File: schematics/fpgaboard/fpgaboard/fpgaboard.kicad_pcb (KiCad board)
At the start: 6 copper layers, 67.6 x 37.5 mm, 17 parts, among them J1 SODIMM-200, U1 LFE5UM-85F-8BG381I, U13 W25Q32JVSS, U2 AMS1117-3.3, U3 IS42S16320F-7TL, U4 IS42S16320F-7TL

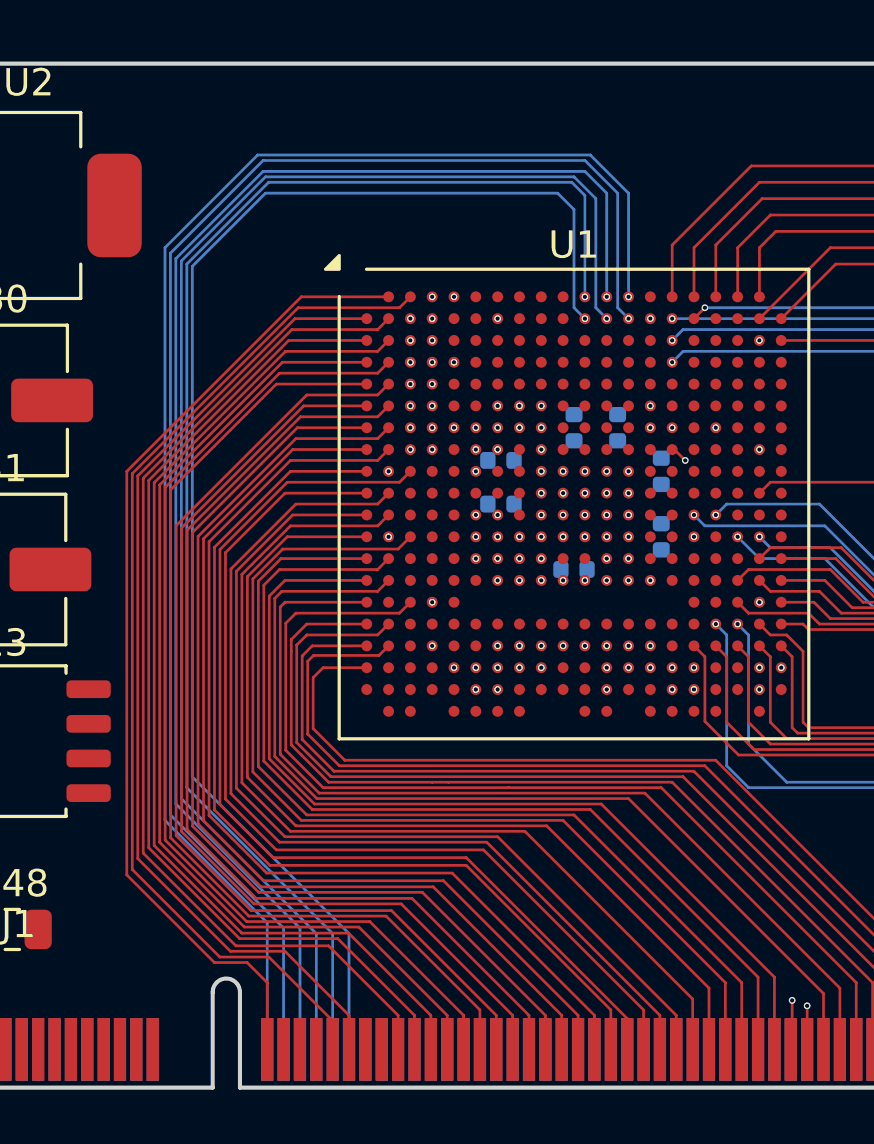
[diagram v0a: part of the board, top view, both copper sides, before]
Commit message: More work on FPGA board.
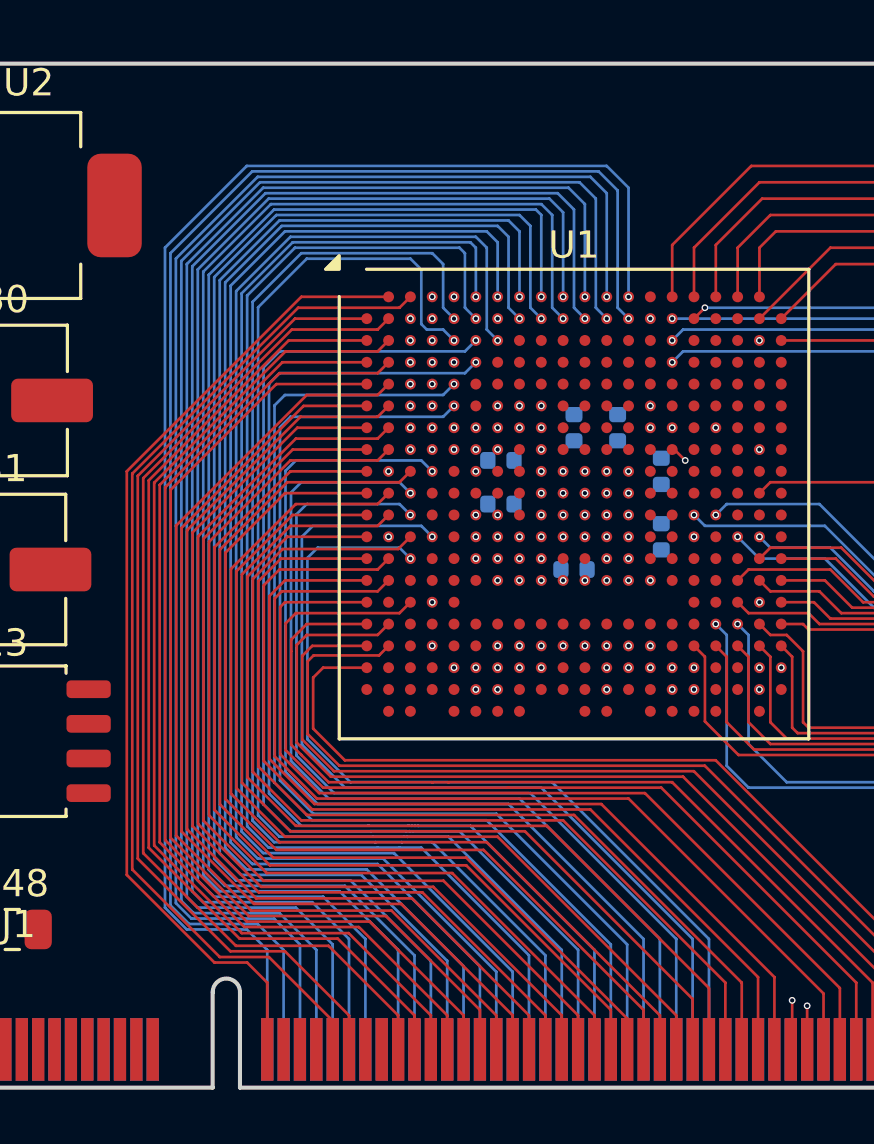
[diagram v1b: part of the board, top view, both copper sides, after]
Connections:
- U1 pad A10: unconnected-(U1B-PT63A-PadA10) -> S58
- U1 pad A6: unconnected-(U1B-PT4A-PadA6) -> S66
- U1 pad A7: unconnected-(U1B-PT18A-PadA7) -> S64
- U1 pad A8: unconnected-(U1B-PT18B-PadA8) -> S62
- U1 pad A9: unconnected-(U1B-PT60A-PadA9) -> S60
- U1 pad B10: unconnected-(U1B-PT60B-PadB10) -> S59
- U1 pad B5: unconnected-(U1G-PL11C-PadB5) -> S68
- U1 pad B6: unconnected-(U1B-PT4B-PadB6) -> S67
- U1 pad B8: unconnected-(U1B-PT15B-PadB8) -> S63
- U1 pad B9: unconnected-(U1B-PT58A-PadB9) -> S61
- U1 pad C5: unconnected-(U1G-PL11D-PadC5) -> S69
- U1 pad C6: unconnected-(U1B-PT11A-PadC6) -> S70
- U1 pad C7: unconnected-(U1B-PT11B-PadC7) -> S65
- U1 pad D6: unconnected-(U1B-PT6B-PadD6) -> S71
- U1 pad E5: unconnected-(U1G-PL20C-PadE5) -> S72
- U1 pad F5: unconnected-(U1G-PL20D-PadF5) -> S73
- U1 pad H5: unconnected-(U1G-PL41C-PadH5) -> S74
- U1 pad J4: unconnected-(U1F-PL50A-PadJ4) -> S74
- U1 pad K3: unconnected-(U1F-PL50D-PadK3) -> S75
- U1 pad L3: unconnected-(U1F-PL86C-PadL3) -> S76
- U1 pad M4: unconnected-(U1F-PL83A-PadM4) -> S77
- U1 pad N3: unconnected-(U1F-PL86A-PadN3) -> S78
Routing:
- net S59: track 0.00 -> 52.0 mm, vias 0 -> 1
- net S58: track 0.00 -> 51.3 mm, vias 0 -> 1
- net S60: track 0.00 -> 50.4 mm, vias 0 -> 1
- net S61: track 0.00 -> 50.3 mm, vias 0 -> 1
- net S63: track 0.00 -> 48.9 mm, vias 0 -> 1
- net S62: track 0.00 -> 48.7 mm, vias 0 -> 1
- net S65: track 0.00 -> 48.2 mm, vias 0 -> 1
- net S64: track 0.00 -> 47.3 mm, vias 0 -> 1
- net S67: track 0.00 -> 46.6 mm, vias 0 -> 1
- net S66: track 0.00 -> 45.9 mm, vias 0 -> 1
- net S69: track 0.00 -> 45.8 mm, vias 0 -> 1
- net S68: track 0.00 -> 45.3 mm, vias 0 -> 1
- net S70: track 0.00 -> 41.6 mm, vias 0 -> 1
- net S71: track 0.00 -> 40.9 mm, vias 0 -> 1
- net S72: track 0.00 -> 39.4 mm, vias 0 -> 1
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
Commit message: Some work on FPGA board.
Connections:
- U1 pad D7: unconnected-(U1B-PT9B-PadD7) -> S86
- U1 pad E6: unconnected-(U1B-PT6A-PadE6) -> S85
- U1 pad J4: S74 -> S75
- U1 pad K3: S75 -> S76
- U1 pad K4: unconnected-(U1F-PL56A-PadK4) -> S77
- U1 pad L3: S76 -> S78
- U1 pad L4: unconnected-(U1F-PL56C-PadL4) -> S79
- U1 pad M4: S77 -> S80
- U1 pad N3: S78 -> S81
- U1 pad N4: unconnected-(U1F-PL83C-PadN4) -> S82
- U1 pad N5: unconnected-(U1F-PL83B-PadN5) -> S83
- U1 pad P5: unconnected-(U1F-PL83D-PadP5) -> S84
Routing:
- net S86: track 0.00 -> 37.5 mm, vias 0 -> 2
- net S85: track 0.00 -> 36.7 mm, vias 0 -> 2
- net S83: track 0.00 -> 34.8 mm, vias 0 -> 1
- net S84: track 0.00 -> 34.6 mm, vias 0 -> 1
- net S79: track 0.00 -> 34.2 mm, vias 0 -> 1
- net S80: track 0.00 -> 33.7 mm, vias 0 -> 1
- net S82: track 0.00 -> 33.3 mm, vias 0 -> 1
- net S81: track 0.00 -> 32.5 mm, vias 0 -> 1
- net S78: track 32.6 -> 33.5 mm
- net S77: track 34.1 -> 34.8 mm
- net S70: track 41.6 -> 41.0 mm
- net S75: track 34.8 -> 35.3 mm
- net S74: track 36.5 -> 36.8 mm, vias 2 -> 1

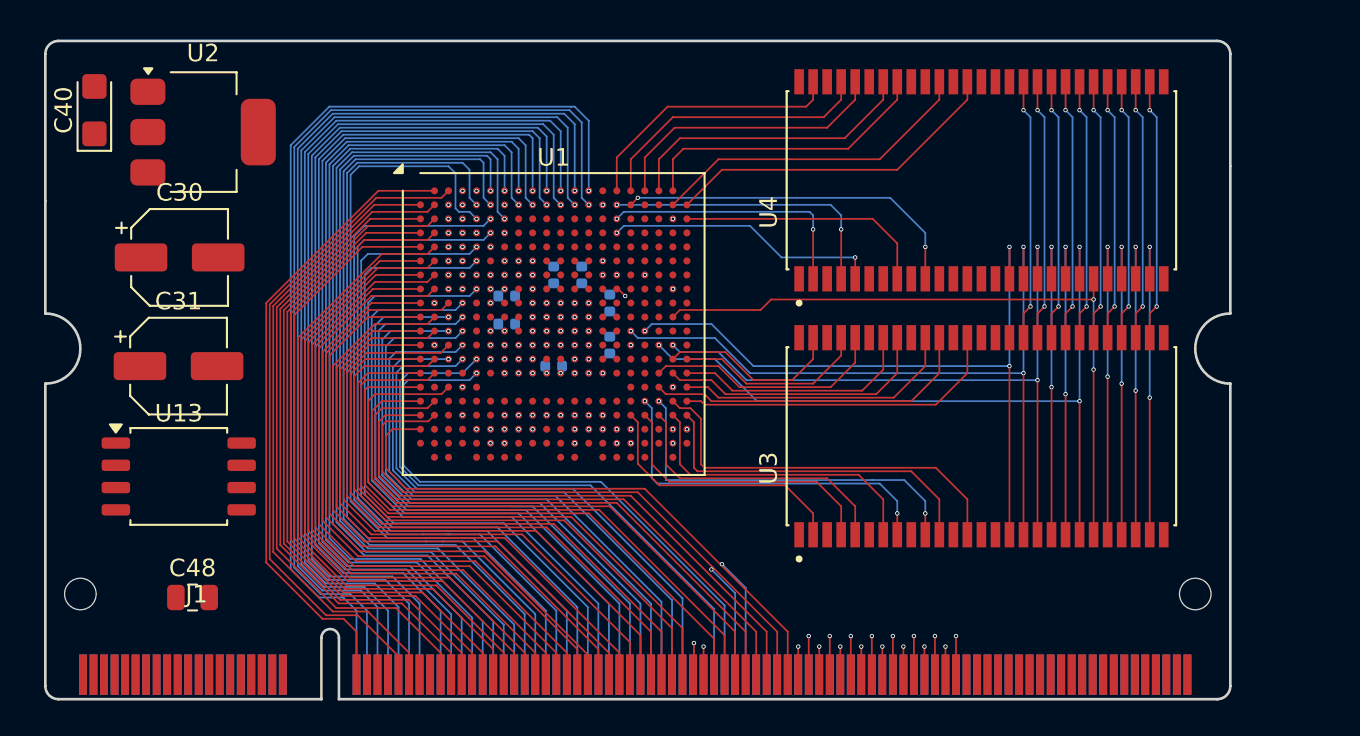
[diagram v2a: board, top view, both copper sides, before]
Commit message: SODIMM connector fully wired up to FPGA.
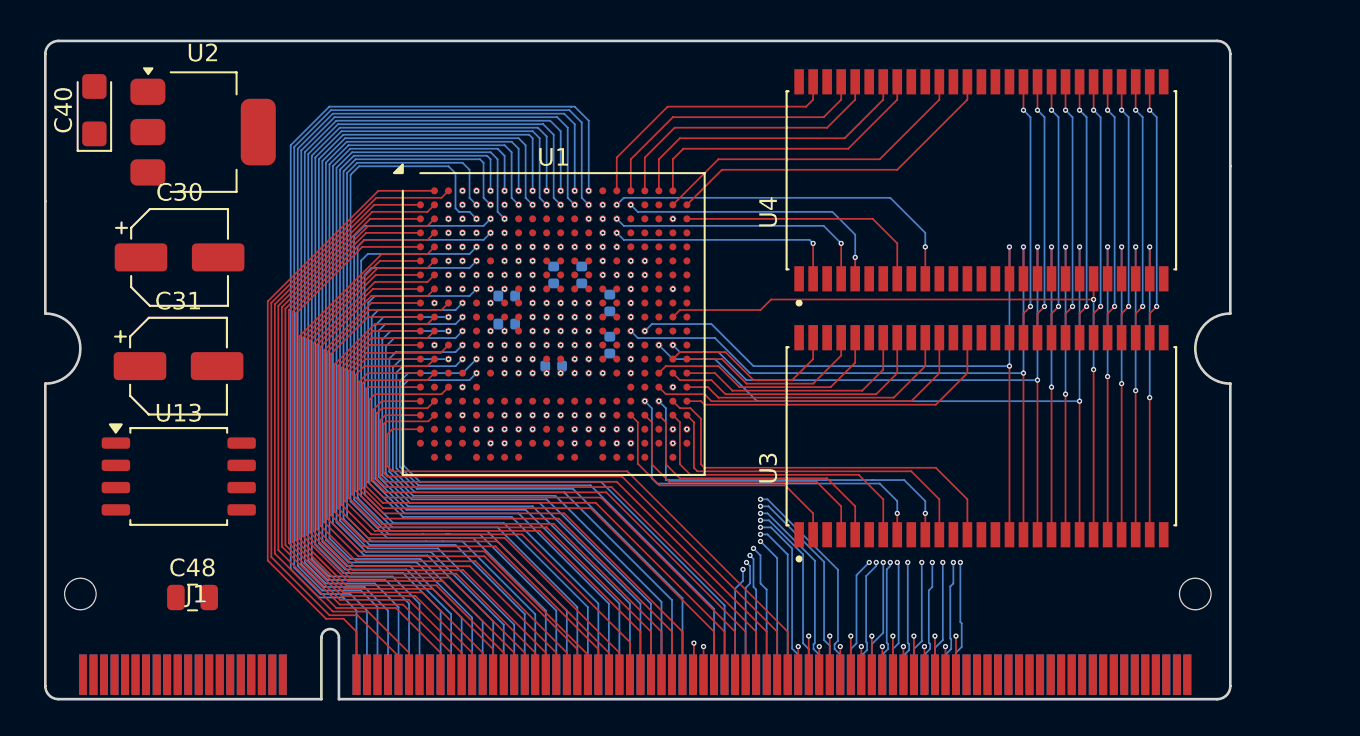
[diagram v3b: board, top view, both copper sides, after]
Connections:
- U1 pad B15: RAM_D17 -> RAM_D21
- U1 pad B16: RAM_D21 -> RAM_D18
- U1 pad C13: unconnected-(U1C-PT78B-PadC13) -> S105
- U1 pad C14: unconnected-(U1C-PT83B-PadC14) -> S106
- U1 pad C15: RAM_D16 -> RAM_D17
- U1 pad D14: unconnected-(U1C-PT85A-PadD14) -> S104
- U1 pad D15: RAM_D18 -> RAM_D16
- U1 pad D20: unconnected-(U1D-PR35C-PadD20) -> RAM_D19
- U1 pad E10: unconnected-(U1B-PT56B-PadE10) -> S90
- U1 pad E11: unconnected-(U1C-PT69B-PadE11) -> S91
- U1 pad E12: unconnected-(U1C-PT74B-PadE12) -> S92
- U1 pad E13: unconnected-(U1C-PT80B-PadE13) -> S93
- U1 pad E14: unconnected-(U1C-PT85B-PadE14) -> S94
- U1 pad E15: RAM_D19 -> S103
- U1 pad E7: unconnected-(U1B-PT9A-PadE7) -> S87
- U1 pad E8: unconnected-(U1B-PT13A-PadE8) -> S88
- U1 pad E9: unconnected-(U1B-PT20B-PadE9) -> S89
- U1 pad F16: unconnected-(U1D-PR11D-PadF16) -> S95
- U1 pad F17: unconnected-(U1D-PR17A-PadF17) -> S102
- U1 pad G16: unconnected-(U1D-PR17C-PadG16) -> S101
- U1 pad H16: unconnected-(U1D-PR17D-PadH16) -> S100
- U1 pad J16: unconnected-(U1D-PR20D-PadJ16) -> S99
- U1 pad K16: unconnected-(U1D-PR29A-PadK16) -> S98
- U1 pad N16: unconnected-(U1E-PR53A-PadN16) -> S97
- U1 pad P16: unconnected-(U1E-PR56B-PadP16) -> S96
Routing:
- net S105: track 0.00 -> 39.1 mm, vias 0 -> 2
- net S106: track 0.00 -> 38.9 mm, vias 0 -> 2
- net S87: track 0.00 -> 37.4 mm, vias 0 -> 2
- net S88: track 0.00 -> 37.3 mm, vias 0 -> 2
- net S89: track 0.00 -> 37.2 mm, vias 0 -> 2
- net S104: track 0.00 -> 37.2 mm, vias 0 -> 2
- net S90: track 0.00 -> 37.1 mm, vias 0 -> 2
- net S91: track 0.00 -> 36.7 mm, vias 0 -> 2
- net S92: track 0.00 -> 36.0 mm, vias 0 -> 2
- net S93: track 0.00 -> 35.4 mm, vias 0 -> 2
- net S103: track 0.00 -> 35.4 mm, vias 0 -> 2
- net S94: track 0.00 -> 34.8 mm, vias 0 -> 2
- net S95: track 0.00 -> 33.7 mm, vias 0 -> 2
- net S102: track 0.00 -> 32.8 mm, vias 0 -> 2
- net S101: track 0.00 -> 32.7 mm, vias 0 -> 2
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
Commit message: Work on connecting up SDRAM to FPGA.
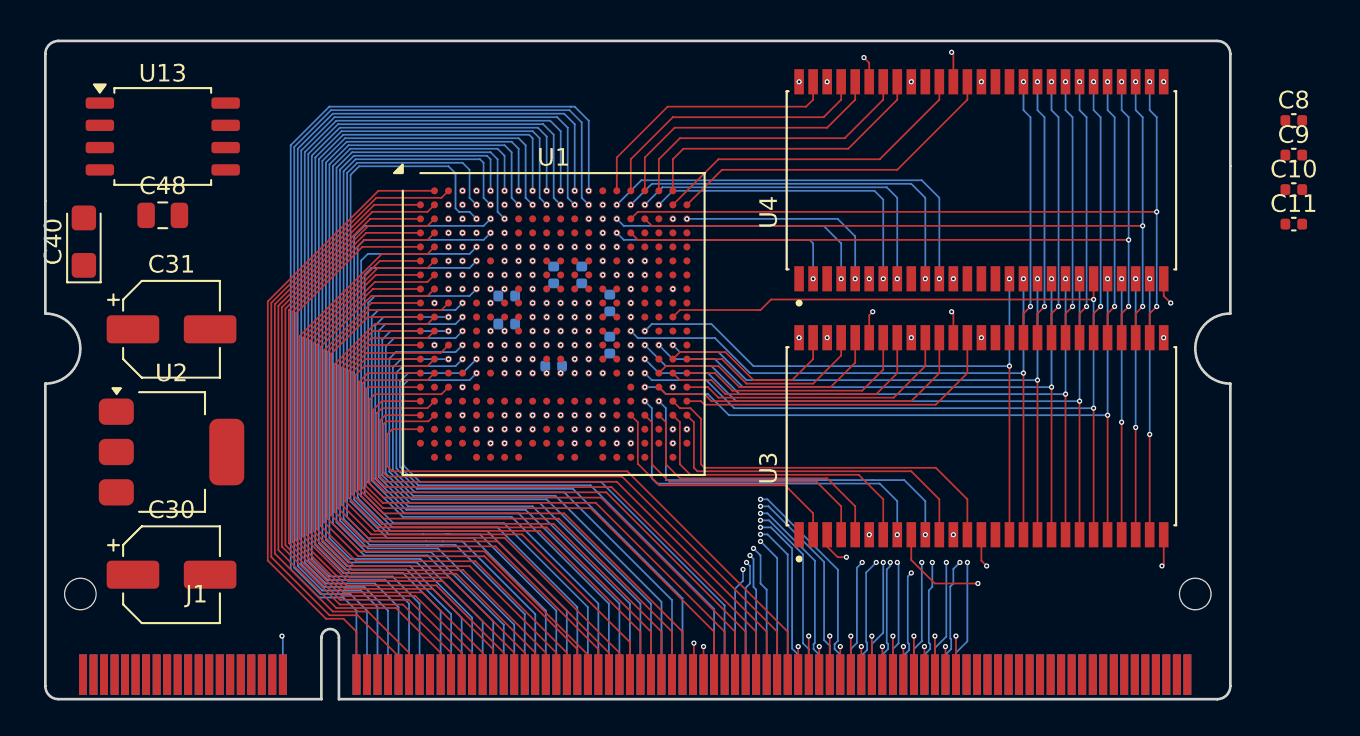
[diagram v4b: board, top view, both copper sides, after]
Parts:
- added C10: C_Small, Capacitor_SMD:C_0402_1005Metric, F.Cu at (191.0, 68.5)
- added C11: C_Small, Capacitor_SMD:C_0402_1005Metric, F.Cu at (191.0, 70.5)
- added C8: C_Small, Capacitor_SMD:C_0402_1005Metric, F.Cu at (191.0, 64.6)
- added C9: C_Small, Capacitor_SMD:C_0402_1005Metric, F.Cu at (191.0, 66.6)
- moved C48 21.9 mm to (126.5, 70.0)
- moved U13 19.4 mm to (126.5, 65.5)
- moved U2 18.3 mm to (127.0, 83.5)
- moved C30 18.1 mm to (127.0, 90.5)
- moved C40 7.52 mm to (122.0, 71.5)
- moved C31 2.14 mm to (127.0, 76.5)
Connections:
- U1 pad B15: RAM_D21 -> RAM_D22
- U1 pad B16: RAM_D18 -> RAM_D21
- U1 pad B17: unconnected-(U1C-PT114A-PadB17) -> RAM_D20
- U1 pad B18: unconnected-(U1C-PT116B-PadB18) -> RAM_D19
- U1 pad B19: RAM_D25 -> unconnected-(U1C-PT119B-PadB19)
- U1 pad C16: RAM_D22 -> RAM_A4
- U1 pad C17: RAM_D26 -> RAM_A5
- U1 pad C20: RAM_D20 -> RAM_D18
- U1 pad D16: RAM_D23 -> RAM_A6
- U1 pad D20: RAM_D19 -> unconnected-(U1D-PR35C-PadD20)
- U1 pad E19: RAM_A0 -> unconnected-(U1D-PR35D-PadE19)
- U1 pad K19: RAM_A10 -> unconnected-(U1D-PR44B-PadK19)
- U1 pad L18: RAM_BA0 -> unconnected-(U1E-PR50C-PadL18)
- U1 pad L19: ~{RAM_CS} -> unconnected-(U1E-PR47C-PadL19)
- U1 pad M17: unconnected-(U1E-PR53B-PadM17) -> RAM_BA0
- U1 pad M18: RAM_BA1 -> ~{RAM_CS}
- U1 pad N17: unconnected-(U1E-PR56A-PadN17) -> RAM_BA1
- U1 pad P17: unconnected-(U1E-PR53D-PadP17) -> RAM_A10
- U1 pad R17: unconnected-(U1E-PR56D-PadR17) -> RAM_A0
- U3 pad 1: Net-(U3-VDD-Pad1) -> IO_3v3
- U3 pad 12: Net-(U3-VSSQ-Pad12) -> GND
- U3 pad 14: Net-(U3-VDD-Pad1) -> IO_3v3
- U3 pad 27: Net-(U3-VDD-Pad1) -> IO_3v3
- U3 pad 28: Net-(U3-VSS-Pad28) -> GND
- U3 pad 3: Net-(U3-VDDQ-Pad3) -> IO_3v3
- U3 pad 41: Net-(U3-VSS-Pad28) -> GND
- U3 pad 43: Net-(U3-VDDQ-Pad3) -> IO_3v3
- U3 pad 46: Net-(U3-VSSQ-Pad12) -> GND
- U3 pad 49: Net-(U3-VDDQ-Pad3) -> IO_3v3
- U3 pad 52: Net-(U3-VSSQ-Pad12) -> GND
- U3 pad 54: Net-(U3-VSS-Pad28) -> GND
- U3 pad 6: Net-(U3-VSSQ-Pad12) -> GND
- U3 pad 9: Net-(U3-VDDQ-Pad3) -> IO_3v3
- U4 pad 1: Net-(U4-VDD-Pad1) -> IO_3v3
- U4 pad 12: Net-(U4-VSSQ-Pad12) -> GND
- U4 pad 14: Net-(U4-VDD-Pad1) -> IO_3v3
- U4 pad 27: Net-(U4-VDD-Pad1) -> IO_3v3
- U4 pad 28: Net-(U4-VSS-Pad28) -> GND
- U4 pad 3: Net-(U4-VDDQ-Pad3) -> IO_3v3
- U4 pad 41: Net-(U4-VSS-Pad28) -> GND
- U4 pad 43: Net-(U4-VDDQ-Pad3) -> IO_3v3
- U4 pad 46: Net-(U4-VSSQ-Pad12) -> GND
- U4 pad 49: Net-(U4-VDDQ-Pad3) -> IO_3v3
- U4 pad 52: Net-(U4-VSSQ-Pad12) -> GND
- U4 pad 54: Net-(U4-VSS-Pad28) -> GND
- U4 pad 6: Net-(U4-VSSQ-Pad12) -> GND
- U4 pad 9: Net-(U4-VDDQ-Pad3) -> IO_3v3
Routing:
- net RAM_A4: track 14.9 -> 45.1 mm, vias 2 -> 3
- net RAM_A6: track 14.9 -> 43.5 mm, vias 2 -> 3
- net RAM_A5: track 14.9 -> 43.5 mm, vias 2 -> 3
- net RAM_A10: track 39.0 -> 65.4 mm, vias 2 -> 3
- net RAM_D22: track 0.00 -> 24.0 mm, vias 0 -> 2
- net RAM_A0: track 18.2 -> 41.7 mm, vias 2 -> 3
- net RAM_BA0: track 18.2 -> 39.8 mm, vias 2 -> 3
- net ~{RAM_CS}: track 18.2 -> 38.0 mm, vias 2 -> 3
- net IO_3v3: track 0.00 -> 19.4 mm, vias 9 -> 18
- net RAM_D19: track 0.00 -> 17.9 mm, vias 0 -> 2
- net RAM_D20: track 14.6 -> 19.7 mm, vias 0 -> 2
- net ~{RAM_WE}: track 40.2 -> 36.6 mm
- net ~{RAM_RAS}: track 39.9 -> 36.2 mm
- net ~{RAM_CAS}: track 41.6 -> 38.0 mm
- net RAM_A3: track 18.2 -> 14.6 mm
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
